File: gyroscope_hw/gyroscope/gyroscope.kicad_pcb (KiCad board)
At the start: 2 copper layers, 59.8 x 26.8 mm, 56 parts, among them Q1 YJL2305A, Q2 LED_5050, Q3 YJL2305A, U1 STM32F103C8Tx

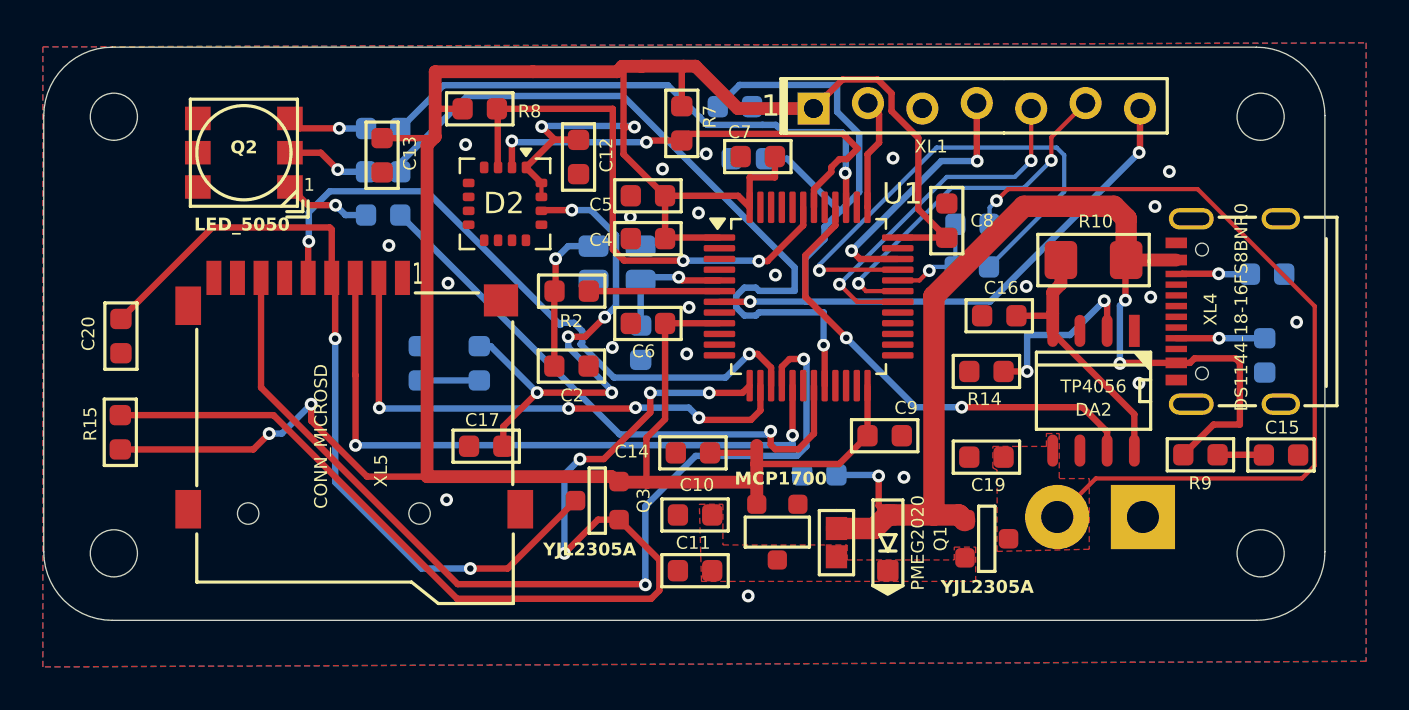
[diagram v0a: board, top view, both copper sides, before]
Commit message: Added firmware and correct PCB
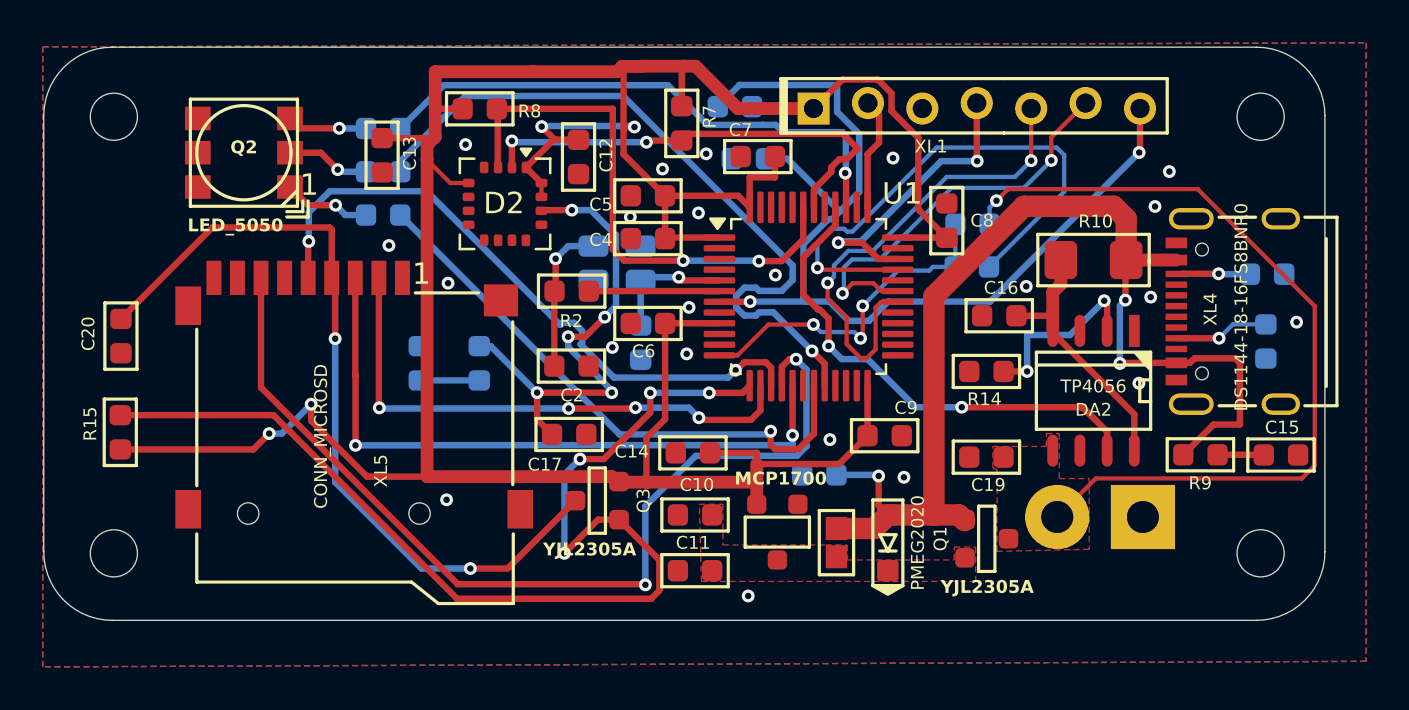
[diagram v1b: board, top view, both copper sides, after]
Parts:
- moved C17 3.91 mm to (155.6, 96.7), turned to 0 degrees
- moved R11 0.65 mm to (188.2, 92.4)
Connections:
- D2 pad 5: GND -> +3v3
- U1 pad 12: unconnected-(U1-PA2-Pad12) -> /ADC_BAT
- U1 pad 32: /ADC_BAT -> unconnected-(U1-PA11-Pad32)
- U1 pad 44: unconnected-(U1-BOOT0-Pad44) -> GND
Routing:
- net /ADC_BAT: track 4.92 -> 16.1 mm, vias 1 -> 3
- net /PRG.UART1_MCU_TX: track 16.8 -> 22.7 mm
- net /PRG.UART1_MCU_RX: track 16.8 -> 19.3 mm
- net +3v3: track 147.8 -> 149.7 mm
- net /LED_R: track 35.8 -> 34.0 mm
- net /PRG.SWDIO: track 12.6 -> 13.9 mm
- net /RST: track 46.6 -> 47.5 mm
- net Net-(D2-PLLFIT): track 23.8 -> 22.9 mm
- net /IS_CHARGING: track 22.3 -> 23.2 mm
- net /ADC_BAT_EN: track 24.5 -> 25.2 mm
- net GND: vias 21 -> 22
